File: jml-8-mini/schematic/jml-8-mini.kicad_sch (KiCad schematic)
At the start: 11 parts, among them J6 Z80 Lines, U1 Z80CPU

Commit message: change "JML-8 Mini" to "JML-8-Mini" in schematic description
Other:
- title: JML-8 Mini Schematic -> JML-8-Mini Schematic
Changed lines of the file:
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@@
   (paper "A4")
   (title_block
-    (title "JML-8 Mini Schematic")
+    (title "JML-8-Mini Schematic")
     (date "2023-10-02")
     (rev "A")

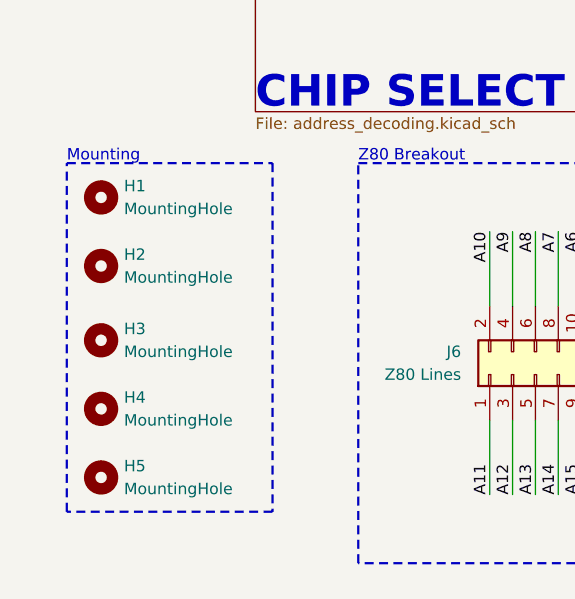
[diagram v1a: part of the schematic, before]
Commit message: Rev B, change dimensions of PCB for reduced cost
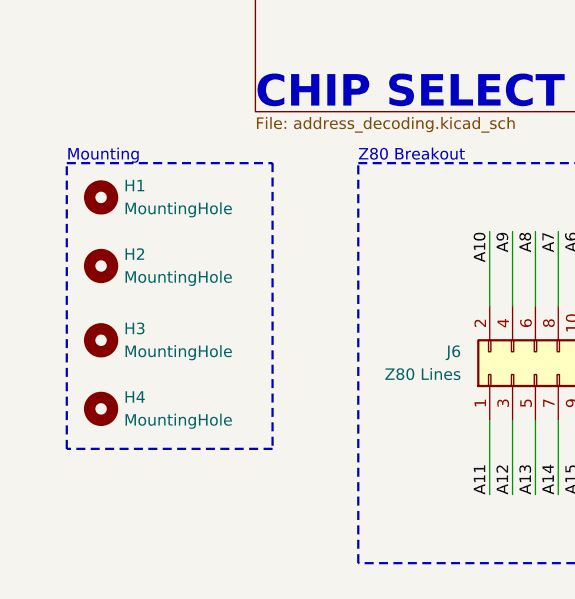
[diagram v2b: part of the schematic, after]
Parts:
- removed H5: MountingHole, MountingHole:MountingHole_3.2mm_M3, symbol Mechanical:MountingHole
- H1, H2, H3, H4: footprint MountingHole:MountingHole_3.2mm_M3 -> MountingHole:MountingHole_2.7mm_M2.5
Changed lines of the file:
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@@
   (title_block
     (title "JML-8-Mini Schematic")
-    (date "2023-10-02")
-    (rev "A")
+    (date "2023-10-20")
+    (rev "B")
     (company "https://github.com/jac-oblong/JML")
     (comment 1 "Design of Z80 based microcomputer")
@@
     (fill (type none))
   )
-  (rectangle (start 15.24 150.495) (end 38.1 189.23)
+  (rectangle (start 15.24 150.495) (end 38.1 182.245)
     (stroke (width 0.25) (type dash_dot_dot))
     (fill (type none))
@@
       (effects (font (size 1.27 1.27)) (justify left))
     )
-    (property "Footprint" "MountingHole:MountingHole_3.2mm_M3" (at 19.05 170.18 0)
+    (property "Footprint" "MountingHole:MountingHole_2.7mm_M2.5" (at 19.05 170.18 0)
       (effects (font (size 1.27 1.27)) hide)
     )
@@
         (path "/7f93abb4-2372-4a9e-a664-5edb67349db4"
           (reference "#G1") (unit 1)
-        )
-      )
-    )
-  )
-  (symbol (lib_id "Mechanical:MountingHole") (at 19.05 185.42 0) (unit 1)
-    (in_bom yes) (on_board yes) (dnp no) (fields_autoplaced)
-    (property "Reference" "H5" (at 21.59 184.15 0)
-      (effects (font (size 1.27 1.27)) (justify left))
-    )
-    (property "Value" "MountingHole" (at 21.59 186.69 0)
-      (effects (font (size 1.27 1.27)) (justify left))
-    )
-    (property "Footprint" "MountingHole:MountingHole_3.2mm_M3" (at 19.05 185.42 0)
-      (effects (font (size 1.27 1.27)) hide)
-    )
-    (property "Datasheet" "~" (at 19.05 185.42 0)
-      (effects (font (size 1.27 1.27)) hide)
-    )
-    (instances
-      (project "jml-8-mini"
-        (path "/7f93abb4-2372-4a9e-a664-5edb67349db4"
-          (reference "H5") (unit 1)
         )
       )
@@
       (effects (font (size 1.27 1.27)) (justify left))
     )
-    (property "Footprint" "MountingHole:MountingHole_3.2mm_M3" (at 19.05 177.8 0)
+    (property "Footprint" "MountingHole:MountingHole_2.7mm_M2.5" (at 19.05 177.8 0)
       (effects (font (size 1.27 1.27)) hide)
     )
@@
       (effects (font (size 1.27 1.27)) (justify left))
     )
-    (property "Footprint" "MountingHole:MountingHole_3.2mm_M3" (at 19.05 154.305 0)
+    (property "Footprint" "MountingHole:MountingHole_2.7mm_M2.5" (at 19.05 154.305 0)
       (effects (font (size 1.27 1.27)) hide)
     )
@@
       (effects (font (size 1.27 1.27)) (justify left))
     )
-    (property "Footprint" "MountingHole:MountingHole_3.2mm_M3" (at 19.05 161.925 0)
-      (effects (font (size 1.27 1.27)) hide)
-    )
+    (property "Footprint" "MountingHole:MountingHole_2.7mm_M2.5" (at 19.05 161.925 0)
+      (effects (font (size 1.27 1.27)) hide)
+    )

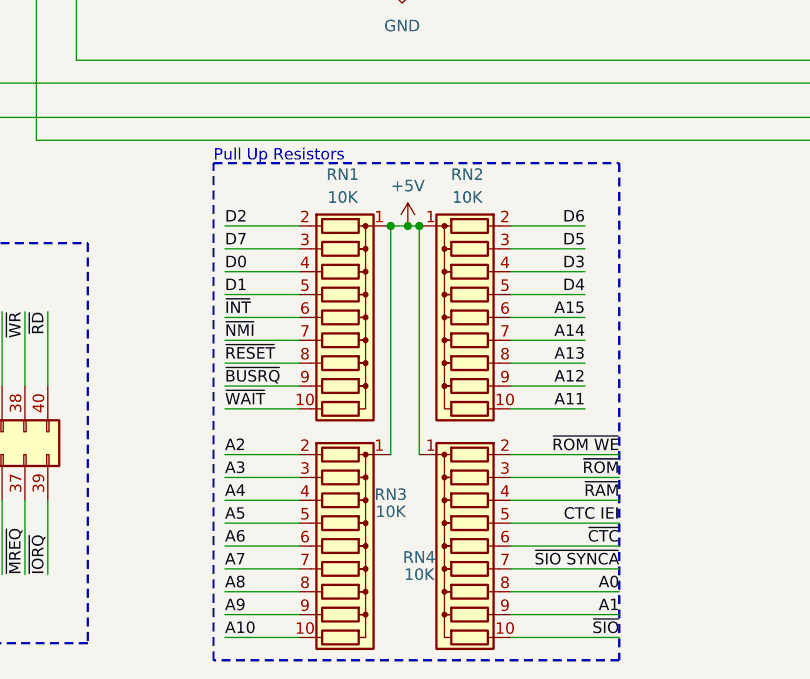
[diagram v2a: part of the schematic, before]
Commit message: finish rerouting PCB for Rev B
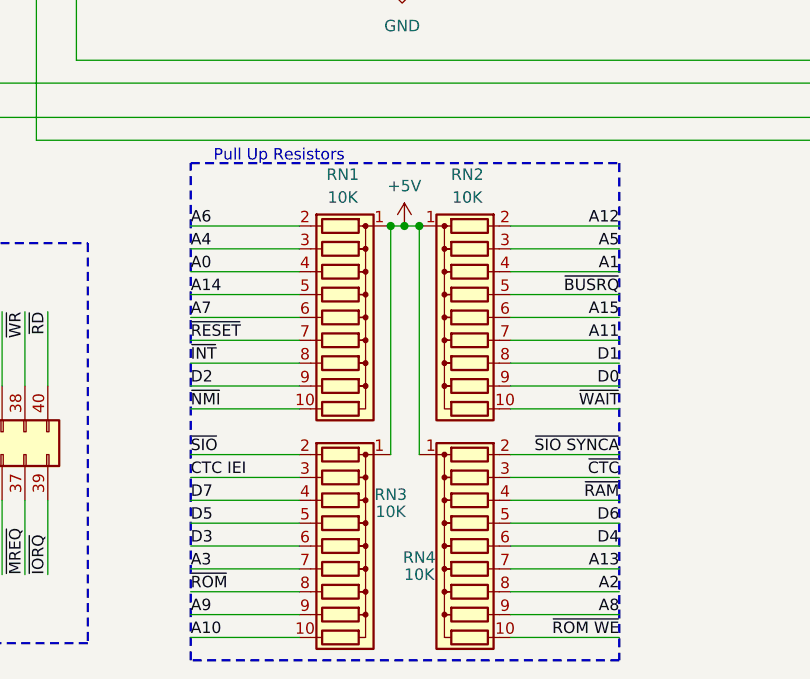
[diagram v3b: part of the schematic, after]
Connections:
- net A0: now also RN1.4 (R3); no longer RN4.8 (R7)
- net A1: now also RN2.4 (R3); no longer RN4.9 (R8)
- net A11: now also RN2.7 (R6); no longer RN2.10 (R9)
- net A12: now also RN2.2 (R1); no longer RN2.9 (R8)
- net A13: now also RN4.7 (R6); no longer RN2.8 (R7)
- net A14: now also RN1.5 (R4); no longer RN2.7 (R6)
- net A2: now also RN4.8 (R7); no longer RN3.2 (R1)
- net A3: now also RN3.7 (R6); no longer RN3.3 (R2)
- net A4: now also RN1.3 (R2); no longer RN3.4 (R3)
- net A5: now also RN2.3 (R2); no longer RN3.5 (R4)
- net A6: now also RN1.2 (R1); no longer RN3.6 (R5)
- net A7: now also RN1.6 (R5); no longer RN3.7 (R6)
- net A8: now also RN4.9 (R8); no longer RN3.8 (R7)
- net CTC IEI: now also RN3.3 (R2); no longer RN4.5 (R4)
- net D0: now also RN2.9 (R8); no longer RN1.4 (R3)
- net D1: now also RN2.8 (R7); no longer RN1.5 (R4)
- net D2: now also RN1.9 (R8); no longer RN1.2 (R1)
- net D3: now also RN3.6 (R5); no longer RN2.4 (R3)
- net D4: now also RN4.6 (R5); no longer RN2.5 (R4)
- net D5: now also RN3.5 (R4); no longer RN2.3 (R2)
- net D6: now also RN4.5 (R4); no longer RN2.2 (R1)
- net D7: now also RN3.4 (R3); no longer RN1.3 (R2)
- net ~{BUSRQ}: now also RN2.5 (R4); no longer RN1.9 (R8)
- net ~{CTC}: now also RN4.3 (R2); no longer RN4.6 (R5)
- net ~{INT}: now also RN1.8 (R7); no longer RN1.6 (R5)
- net ~{NMI}: now also RN1.10 (R9); no longer RN1.7 (R6)
- net ~{RESET}: now also RN1.7 (R6); no longer RN1.8 (R7)
- net ~{ROM WE}: now also RN4.10 (R9); no longer RN4.2 (R1)
- net ~{ROM}: now also RN3.8 (R7); no longer RN4.3 (R2)
- net ~{SIO SYNCA}: now also RN4.2 (R1); no longer RN4.7 (R6)
- net ~{SIO}: now also RN3.2 (R1); no longer RN4.10 (R9)
- net ~{WAIT}: now also RN2.10 (R9); no longer RN1.10 (R9)
